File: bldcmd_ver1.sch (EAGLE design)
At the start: 91 parts, among them CN1 DF61-2P-2.2V(23), CN2 DF65-3P-1.7V(21), CN3 SM05B-SRSS-TB, CN5 SM04B-SRSS-TB, CN6 SM05B-SRSS-TB, CN7 SM04B-SRSS-TB, IC1 STSPIN32F0A, IC2 AS5047P-ATSM, IC3 ADM4852ACPZ-REEL7, Q1 PSMN2R4-30MLD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

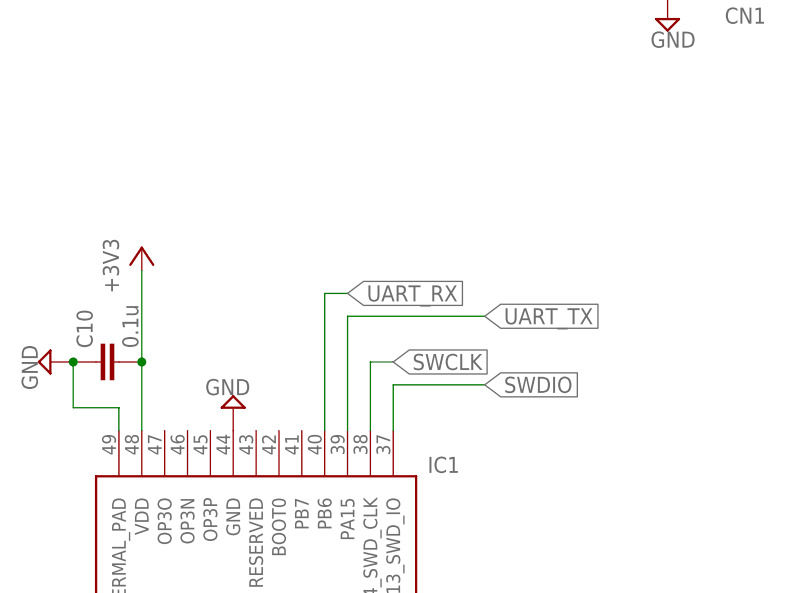
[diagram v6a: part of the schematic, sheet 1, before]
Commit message: BSコンデンサを0402inchに変更 デバッグ用のLEDを追加 BOOT0のプルダウン抵抗の追加( #4)
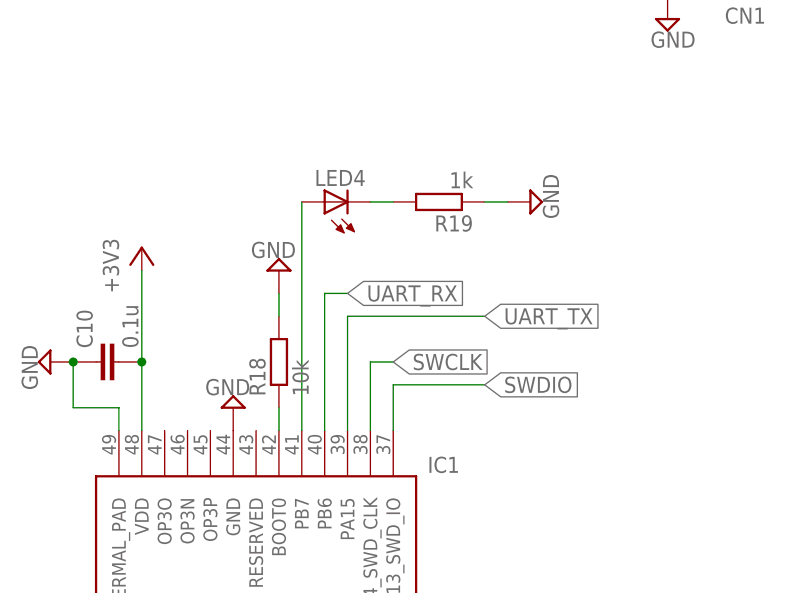
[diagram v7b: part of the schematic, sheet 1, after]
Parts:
- added LED4: (no value), led:LEDSML0603
- added R18: 10k, rcl:R-EU_R0402
- added R19: 1k, rcl:R-EU_R0603
- C1, C2, C3: device rcl:C-EUC0603K -> rcl:C-EUC0402
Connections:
- new net N$22: IC1.BOOT0, R18.1
- new net N$33: LED4.C, R19.2
- new net N$37: IC1.PB7, LED4.A
- net GND: now also R18.2, R19.1
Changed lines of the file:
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@@
 <layer number="19" name="Unrouted" color="6" fill="1" visible="yes" active="no"/>
 <layer number="20" name="Dimension" color="24" fill="1" visible="yes" active="no"/>
-<layer number="21" name="tPlace" color="31" fill="10" visible="yes" active="no"/>
+<layer number="21" name="tPlace" color="31" fill="1" visible="yes" active="no"/>
 <layer number="22" name="bPlace" color="25" fill="10" visible="yes" active="no"/>
 <layer number="23" name="tOrigins" color="15" fill="1" visible="yes" active="no"/>
@@
 <parts>
 <part name="IC1" library="scramble-mcu" deviceset="STSPIN32F0A" device=""/>
-<part name="C1" library="rcl" library_urn="urn:adsk.eagle:library:334" deviceset="C-EU" device="C0603K" package3d_urn="urn:adsk.eagle:package:23680/2" value="0.1u"/>
-<part name="C2" library="rcl" library_urn="urn:adsk.eagle:library:334" deviceset="C-EU" device="C0603K" package3d_urn="urn:adsk.eagle:package:23680/2" value="0.1u"/>
-<part name="C3" library="rcl" library_urn="urn:adsk.eagle:library:334" deviceset="C-EU" device="C0603K" package3d_urn="urn:adsk.eagle:package:23680/2" value="0.1u"/>
+<part name="C1" library="rcl" library_urn="urn:adsk.eagle:library:334" deviceset="C-EU" device="C0402" package3d_urn="urn:adsk.eagle:package:23626/1" value="0.1u"/>
+<part name="C2" library="rcl" library_urn="urn:adsk.eagle:library:334" deviceset="C-EU" device="C0402" package3d_urn="urn:adsk.eagle:package:23626/1" value="0.1u"/>
+<part name="C3" library="rcl" library_urn="urn:adsk.eagle:library:334" deviceset="C-EU" device="C0402" package3d_urn="urn:adsk.eagle:package:23626/1" value="0.1u"/>
 <part name="R1" library="rcl" library_urn="urn:adsk.eagle:library:334" deviceset="R-EU_" device="R0603" package3d_urn="urn:adsk.eagle:package:23555/2" value="20"/>
 <part name="R2" library="rcl" library_urn="urn:adsk.eagle:library:334" deviceset="R-EU_" device="R0603" package3d_urn="urn:adsk.eagle:package:23555/2" value="20"/>
@@
 <part name="CN5" library="scramble-con-jst" deviceset="?M04B-SRSS-TB" device="S"/>
 <part name="D3" library="diode" library_urn="urn:adsk.eagle:library:210" deviceset="BAT60J" device="" package3d_urn="urn:adsk.eagle:package:43461/1"/>
+<part name="R18" library="rcl" library_urn="urn:adsk.eagle:library:334" deviceset="R-EU_" device="R0402" package3d_urn="urn:adsk.eagle:package:23547/1" value="10k"/>
+<part name="SUPPLY30" library="supply2" library_urn="urn:adsk.eagle:library:372" deviceset="GND" device=""/>
+<part name="LED4" library="led" library_urn="urn:adsk.eagle:library:259" deviceset="LED" device="SML0603" package3d_urn="urn:adsk.eagle:package:15832/1"/>
+<part name="R19" library="rcl" library_urn="urn:adsk.eagle:library:334" deviceset="R-EU_" device="R0603" package3d_urn="urn:adsk.eagle:package:23555/2" value="1k"/>
+<part name="SUPPLY31" library="supply2" library_urn="urn:adsk.eagle:library:372" deviceset="GND" device=""/>
 </parts>
 <sheets>
@@
 <instance part="CN5" gate="G$1" x="-147.32" y="30.48" rot="MR0"/>
 <instance part="D3" gate="G$1" x="-132.08" y="30.48"/>
+<instance part="R18" gate="G$1" x="33.02" y="35.56" rot="R90"/>
+<instance part="SUPPLY30" gate="GND" x="33.02" y="45.72" rot="R180"/>
+<instance part="LED4" gate="G$1" x="38.1" y="53.34" rot="R90"/>
+<instance part="R19" gate="G$1" x="50.8" y="53.34" rot="R180"/>
+<instance part="SUPPLY31" gate="GND" x="60.96" y="53.34" rot="R90"/>
 </instances>
 <busses>
@@
 <pinref part="SUPPLY26" gate="GND" pin="GND"/>
 </segment>
+<segment>
+<pinref part="SUPPLY30" gate="GND" pin="GND"/>
+<pinref part="R18" gate="G$1" pin="2"/>
+<wire x1="33.02" y1="43.18" x2="33.02" y2="40.64" width="0.1524" layer="91"/>
+</segment>
+<segment>
+<pinref part="SUPPLY31" gate="GND" pin="GND"/>
+<pinref part="R19" gate="G$1" pin="1"/>
+<wire x1="58.42" y1="53.34" x2="55.88" y2="53.34" width="0.1524" layer="91"/>
+</segment>
 </net>
 <net name="+3V3" class="0">
@@
 </segment>
 </net>
+<net name="N$22" class="0">
+<segment>
+<pinref part="R18" gate="G$1" pin="1"/>
+<pinref part="IC1" gate="G$1" pin="BOOT0"/>
+<wire x1="33.02" y1="30.48" x2="33.02" y2="27.94" width="0.1524" layer="91"/>
+</segment>
+</net>
+<net name="N$33" class="0">
+<segment>
+<pinref part="R19" gate="G$1" pin="2"/>
+<pinref part="LED4" gate="G$1" pin="C"/>
+<wire x1="45.72" y1="53.34" x2="43.18" y2="53.34" width="0.1524" layer="91"/>
+</segment>
+</net>
+<net name="N$37" class="0">
+<segment>
+<pinref part="LED4" gate="G$1" pin="A"/>
+<pinref part="IC1" gate="G$1" pin="PB7"/>
+<wire x1="35.56" y1="53.34" x2="35.56" y2="27.94" width="0.1524" layer="91"/>
+</segment>
+</net>

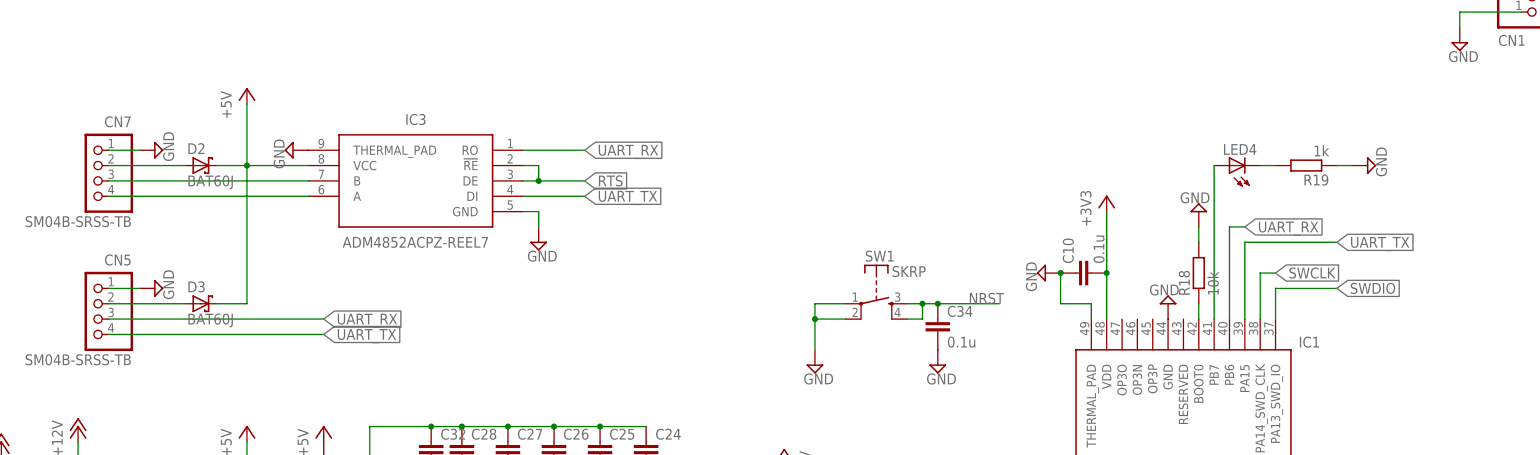
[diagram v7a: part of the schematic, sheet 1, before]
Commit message: RS485のICをSOIC8のものに変更
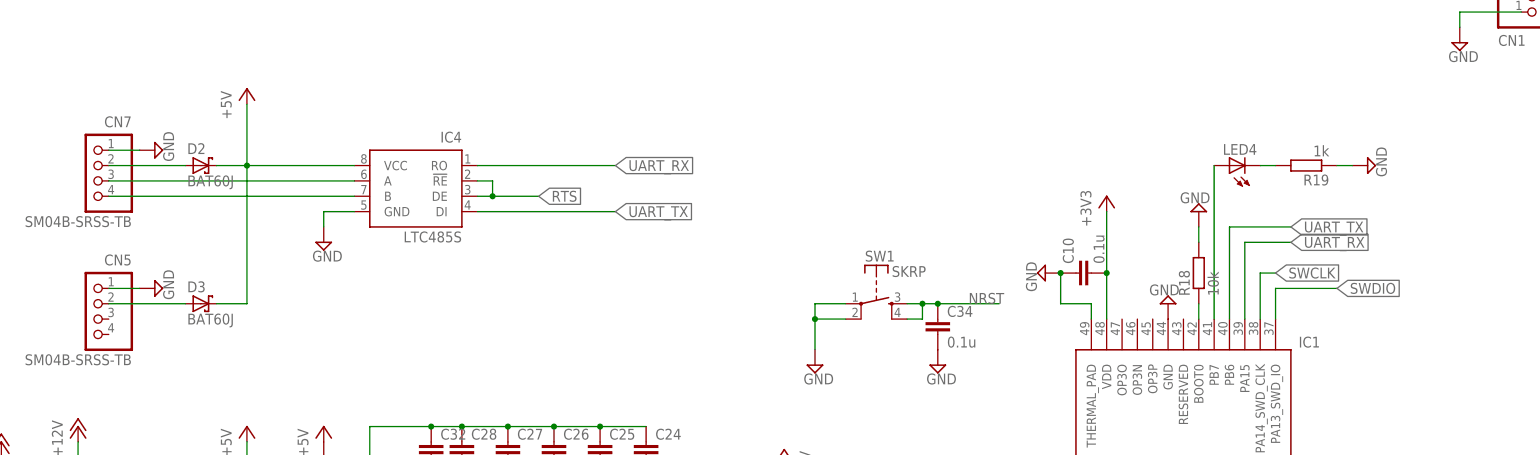
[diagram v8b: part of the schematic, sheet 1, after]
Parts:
- removed IC3: ADM4852ACPZ-REEL7, rcssl_lib:ADM4852ACPZ-REEL7
- added IC4: LTC485S, linear-technology:LTC485S
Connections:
- net +5V: now also IC4.VCC; no longer IC3.VCC
- net GND: now also IC4.GND; no longer IC3.GND, IC3.THERMAL_PAD
- net N$29: now also IC4.A; no longer IC3.B
- net N$32: now also IC4.B; no longer IC3.A
- net RTS: now also IC4.!RE, IC4.DE; no longer IC3.!RE, IC3.DE
- net UART_RX: now also IC1.PA15, IC4.RO; no longer CN5.3, IC1.PB6, IC3.RO
- net UART_TX: now also IC1.PB6, IC4.DI; no longer CN5.4, IC1.PA15, IC3.DI
